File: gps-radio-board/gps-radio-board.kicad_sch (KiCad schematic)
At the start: 21 parts, among them J1 SMA, J2 SMA, J3 USB_C_Receptacle_USB2.0_16P, J4 JST_BATT, U1 ESP32-C6-MINI-1U-H4, U4 AP2112K-3.3, U5 MAX-M10N, U6 MCP73831, U7 AP2112K-3.3

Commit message: Add components to schematic
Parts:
- added C10: 22u, Capacitor_SMD:C_0603_1608Metric_Pad1.08x0.95mm_HandSolder, symbol Device:C
- added C7: 1u, Capacitor_SMD:C_0603_1608Metric_Pad1.08x0.95mm_HandSolder, symbol Device:C
- added C8, C9: 100n, Capacitor_SMD:C_0603_1608Metric_Pad1.08x0.95mm_HandSolder, symbol Device:C
- added D2: LED, LED_SMD:LED_0201_0603Metric_Pad0.64x0.40mm_HandSolder, symbol Device:LED
- added R5: 470, Resistor_SMD:R_0603_1608Metric_Pad0.98x0.95mm_HandSolder, symbol Device:R_US
- added R6, R7: 10k, Resistor_SMD:R_0603_1608Metric_Pad0.98x0.95mm_HandSolder, symbol Device:R_US
- added RST2: SW_Omron_B3FS, Button_Switch_SMD:SW_SPST_Omron_B3FS-100xP, symbol Switch:SW_Omron_B3FS
- J4: footprint Connector_JST:JST_XH_S2B-XH-A-1_1x02_P2.50mm_Horizontal -> Connector_JST:JST_GH_SM02B-GHS-TB_1x02-1MP_P1.25mm_Horizontal
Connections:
- net +BATT: no longer U4.3 (EN)
- net GND: now also C10.1, C7.1, C8.2, C9.1, R5.2, RST2.1
- net WIO_UART_2_RX: now also U1.31 (TXD0); no longer U1.30 (RXD0)
- net WIO_UART_2_TX: now also U1.30 (RXD0); no longer U1.31 (TXD0)
- net EXT_INT_GPS: now reaches U5.5 (EXTINT)
- net EXT_INT_GPS: now also U2.20 (PB10)
- net +3V3: now reaches U5.7 (V_IO)
- net +3V3: now also C1.1, C2.1, C3.1, U2.1 (VCC), U2.28 (VDD), U4.5 (VOUT), U5.8 (VCC)
- net at U1.22 (IO8): now also R7.1
- net at U1.5 (IO2): now also U4.3 (EN)
- net at U1.6 (IO3): now also D2.2 (A)
- net at U1.8 (EN): now also C7.2, C8.1, R6.1, RST2.2
- net SPI-CS: now reaches U2.23 (PA0)
- net +3V3_G renamed +3V3_E
- net +3V3_E: now also U1.3 (3V3), C10.2, C9.2, R6.2, R7.2
- removed net +3V3_R: C1.1, C2.1, C3.1, U1.3 (3V3), U2.1 (VCC), U2.28 (VDD), U4.5 (VOUT)
- new net: D2.1 (K), R5.1
- no-connect marks 2 -> 29
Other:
- note added: "<-Connect if active antenna used"
- note added: "Battery Charger"
- note added: "GPS"
- note added: "Radio"
- note added: "\/-Connect if backup supply is wanted"
- moved on the sheet: C2, C3, C4, J1, J2, J4, R3, U2, U5

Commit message: Inital rousting
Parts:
- removed RST2: SW_Omron_B3FS, Button_Switch_SMD:SW_SPST_Omron_B3FS-100xP, symbol Switch:SW_Omron_B3FS
- added C11, C12: 15p, Capacitor_SMD:C_0603_1608Metric_Pad1.08x0.95mm_HandSolder, symbol Device:C
- added D3, D4: 40V@1A, Diode_SMD:D_SOD-123, symbol Device:D_Schottky
- added J5, J6: Conn_01x04, Connector_JST:JST_SH_BM04B-SRSS-TB_1x04-1MP_P1.00mm_Vertical, symbol Connector_Generic:Conn_01x04
- added J7: Conn_01x04, Connector_PinHeader_2.54mm:PinHeader_1x04_P2.54mm_Vertical, symbol Connector_Generic:Conn_01x04
- added R8, R9: 22, Resistor_SMD:R_0603_1608Metric_Pad0.98x0.95mm_HandSolder, symbol Device:R_US
- D1, D2: footprint LED_SMD:LED_0201_0603Metric_Pad0.64x0.40mm_HandSolder -> LED_SMD:LED_0603_1608Metric_Pad1.05x0.95mm_HandSolder
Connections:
- net +3V3: now also J5.1 (Pin_1), J6.3 (Pin_3)
- net +3V3_E: now also J7.1 (Pin_1)
- net +BATT: now also D3.2 (A); no longer C4.1, C5.1, U4.1 (VIN), U7.1 (VIN), U7.3 (EN)
- net GND: now also C11.1, C12.1, J5.4 (Pin_4), J6.4 (Pin_4), J7.4 (Pin_4)
- net I2C-2-SCA: now also J6.2 (Pin_2)
- net I2C-2-SCL: now also J6.1 (Pin_1)
- net SWD-WIO-CLK: now also J5.3 (Pin_3)
- net SWD-WIO-IO: now also J5.2 (Pin_2)
- net USB_D+: now also C11.2, R8.1; no longer J3.A6 (D+), J3.B6 (D+)
- net USB_D-: now also C12.2, R9.1; no longer J3.A7 (D-), J3.B7 (D-)
- net USB_IN: now also D4.2 (A)
- net at U1.10 (IO5): now also J7.3 (Pin_3)
- net at U1.9 (IO4): now also J7.2 (Pin_2)
- new net: J3.A6 (D+), J3.B6 (D+), R8.2
- new net: C4.1, C5.1, D3.1 (K), D4.1 (K), U4.1 (VIN), U7.1 (VIN), U7.3 (EN)
- new net: J3.A7 (D-), J3.B7 (D-), R9.2
- no-connect marks 29 -> 27
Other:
- moved on the sheet: R7

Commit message: Update silkscreen
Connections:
- net +3V3: now also J5.3 (Pin_3); no longer J5.1 (Pin_1)
- net SWD-WIO-CLK: now also J5.2 (Pin_2); no longer J5.3 (Pin_3)
- net SWD-WIO-IO: now also J5.1 (Pin_1); no longer J5.2 (Pin_2)
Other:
- moved on the sheet: J5
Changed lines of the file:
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@@
 	(wire
 		(pts
+			(xy 591.82 363.22) (xy 594.36 363.22)
+		)
+		(stroke
+			(width 0)
+			(type default)
+		)
+	)
+	(wire
+		(pts
+			(xy 598.17 365.76) (xy 591.82 365.76)
+		)
+		(stroke
+			(width 0)
+			(type default)
+		)
+	)
+	(wire
+		(pts
 			(xy 676.91 228.6) (xy 679.45 228.6)
 		)
@@
 	(wire
 		(pts
-			(xy 590.55 359.41) (xy 594.36 359.41)
-		)
-		(stroke
-			(width 0)
-			(type default)
-		)
-	)
-	(wire
-		(pts
 			(xy 477.52 359.41) (xy 477.52 361.95)
 		)
@@
 	(wire
 		(pts
-			(xy 590.55 356.87) (xy 593.09 356.87)
-		)
-		(stroke
-			(width 0)
-			(type default)
-		)
-	)
-	(wire
-		(pts
 			(xy 571.5 299.72) (xy 565.15 299.72)
 		)
@@
 	(wire
 		(pts
-			(xy 593.09 353.06) (xy 622.3 353.06)
+			(xy 591.82 353.06) (xy 622.3 353.06)
 		)
 		(stroke
@@
 	(wire
 		(pts
-			(xy 593.09 356.87) (xy 593.09 353.06)
+			(xy 591.82 360.68) (xy 591.82 353.06)
 		)
 		(stroke
@@
 	(wire
 		(pts
-			(xy 594.36 359.41) (xy 594.36 355.6)
+			(xy 594.36 363.22) (xy 594.36 355.6)
 		)
 		(stroke
@@
 	)
 	(symbol
-		(lib_id "power:+3V3")
-		(at 590.55 354.33 0)
-		(unit 1)
-		(body_style 1)
-		(exclude_from_sim no)
-		(in_bom yes)
-		(on_board yes)
-		(in_pos_files yes)
-		(dnp no)
-		(fields_autoplaced yes)
-		(property "Reference" "#PWR031"
-			(at 590.55 358.14 0)
-			(hide yes)
-			(show_name no)
-			(do_not_autoplace no)
-			(effects
-				(font
-					(size 1.27 1.27)
-				)
-			)
-		)
-		(property "Value" "+3V3"
-			(at 590.55 349.25 0)
-			(show_name no)
-			(do_not_autoplace no)
-			(effects
-				(font
-					(size 1.27 1.27)
-				)
-			)
-		)
-		(property "Footprint" ""
-			(at 590.55 354.33 0)
-			(hide yes)
-			(show_name no)
-			(do_not_autoplace no)
-			(effects
-				(font
-					(size 1.27 1.27)
-				)
-			)
-		)
-		(property "Datasheet" ""
-			(at 590.55 354.33 0)
-			(hide yes)
-			(show_name no)
-			(do_not_autoplace no)
-			(effects
-				(font
-					(size 1.27 1.27)
-				)
-			)
-		)
-		(property "Description" "Power symbol creates a global label with name \"+3V3\""
-			(at 590.55 354.33 0)
-			(hide yes)
-			(show_name no)
-			(do_not_autoplace no)
-			(effects
-				(font
-					(size 1.27 1.27)
-				)
-			)
-		)
-		(pin "1"
-		)
-		(instances
-			(project "gps-radio-board"
-				(path "/6516832b-56dd-436b-980b-7ee5d107ab91"
-					(reference "#PWR031")
-					(unit 1)
-				)
-			)
-		)
-	)
-	(symbol
 		(lib_id "Device:D_Schottky")
 		(at 501.65 261.62 180)
@@
 	(symbol
 		(lib_id "PCM_SparkFun-PowerSymbol:GND")
-		(at 590.55 361.95 0)
+		(at 591.82 368.3 0)
 		(unit 1)
 		(body_style 1)
@@
 		(fields_autoplaced yes)
 		(property "Reference" "#PWR032"
-			(at 590.55 368.3 0)
+			(at 591.82 374.65 0)
 			(hide yes)
 			(show_name no)
@@
 		)
 		(property "Value" "GND"
-			(at 590.55 365.76 0)
+			(at 591.82 372.11 0)
 			(show_name no)
 			(do_not_autoplace yes)
@@
 		)
 		(property "Footprint" ""
-			(at 590.55 361.95 0)
+			(at 591.82 368.3 0)
 			(hide yes)
 			(show_name no)
@@
 		)
 		(property "Datasheet" ""
-			(at 590.55 361.95 0)
+			(at 591.82 368.3 0)
 			(hide yes)
 			(show_name no)
@@
 		)
 		(property "Description" "Power symbol creates a global label with name \"GND\" , ground"
-			(at 590.55 370.84 0)
+			(at 591.82 377.19 0)
 			(hide yes)
 			(show_name no)
@@
 	(symbol
 		(lib_id "Connector_Generic:Conn_01x04")
-		(at 585.47 356.87 0)
+		(at 586.74 363.22 0)
 		(mirror y)
 		(unit 1)
@@
 		(dnp no)
 		(property "Reference" "J5"
-			(at 580.644 348.742 0)
+			(at 581.914 355.092 0)
 			(show_name no)
 			(do_not_autoplace no)
@@
 		)
 		(property "Value" "Conn_01x04"
-			(at 580.644 351.028 0)
+			(at 581.914 357.378 0)
 			(show_name no)
 			(do_not_autoplace no)
@@
 		)
 		(property "Footprint" "Connector_JST:JST_SH_BM04B-SRSS-TB_1x04-1MP_P1.00mm_Vertical"
-			(at 585.47 356.87 0)
+			(at 586.74 363.22 0)
 			(hide yes)
 			(show_name no)
@@
 		)
 		(property "Datasheet" ""
-			(at 585.47 356.87 0)
+			(at 586.74 363.22 0)
 			(hide yes)
 			(show_name no)
@@
 		)
 		(property "Description" "Generic connector, single row, 01x04, script generated (kicad-library-utils/schlib/autogen/connector/)"
-			(at 585.47 356.87 0)
+			(at 586.74 363.22 0)
 			(hide yes)
 			(show_name no)
@@
 					(unit 1)
 				)
+			)
+		)
+	)
+	(symbol
+		(lib_id "power:+3V3")
+		(at 598.17 365.76 0)
+		(unit 1)
+		(body_style 1)
+		(exclude_from_sim no)
+		(in_bom yes)
+		(on_board yes)
+		(in_pos_files yes)
+		(dnp no)
+		(fields_autoplaced yes)
+		(property "Reference" "#PWR036"
+			(at 598.17 369.57 0)
+			(hide yes)
+			(show_name no)
+			(do_not_autoplace no)
+			(effects
+				(font
+					(size 1.27 1.27)
+				)
+			)
+		)
+		(property "Value" "+3V3"
+			(at 598.17 360.68 0)
+			(show_name no)
+			(do_not_autoplace no)
+			(effects
+				(font
+					(size 1.27 1.27)
+				)
+			)
+		)
+		(property "Footprint" ""
+			(at 598.17 365.76 0)
+			(hide yes)
+			(show_name no)
+			(do_not_autoplace no)
+			(effects
+				(font
+					(size 1.27 1.27)
+				)
+			)
+		)
+		(property "Datasheet" ""
+			(at 598.17 365.76 0)
+			(hide yes)
+			(show_name no)
+			(do_not_autoplace no)
+			(effects
+				(font
+					(size 1.27 1.27)
+				)
+			)
+		)
+		(property "Description" "Power symbol creates a global label with name \"+3V3\""
+			(at 598.17 365.76 0)
+			(hide yes)
+			(show_name no)
+			(do_not_autoplace no)
+			(effects
+				(font
+					(size 1.27 1.27)
+				)
+			)
+		)
+		(pin "1"
+		)
+		(instances
+			(project "gps-radio-board"
+				(path "/6516832b-56dd-436b-980b-7ee5d107ab91"
+					(reference "#PWR036")
+					(unit 1)
+				)

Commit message: Update silkscreen
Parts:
- added D5, D6: LED, LED_SMD:LED_0603_1608Metric_Pad1.05x0.95mm_HandSolder, symbol Device:LED
- added R10, R11: 470, Resistor_SMD:R_0603_1608Metric_Pad0.98x0.95mm_HandSolder, symbol Device:R_US
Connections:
- net GND: now also R10.2, R11.2
- net at U2.21 (PA9): now also D6.2 (A)
- net at U2.27 (PA10): now also D5.2 (A)
- new net: D5.1 (K), R10.1
- new net: D6.1 (K), R11.1
- no-connect marks 27 -> 25

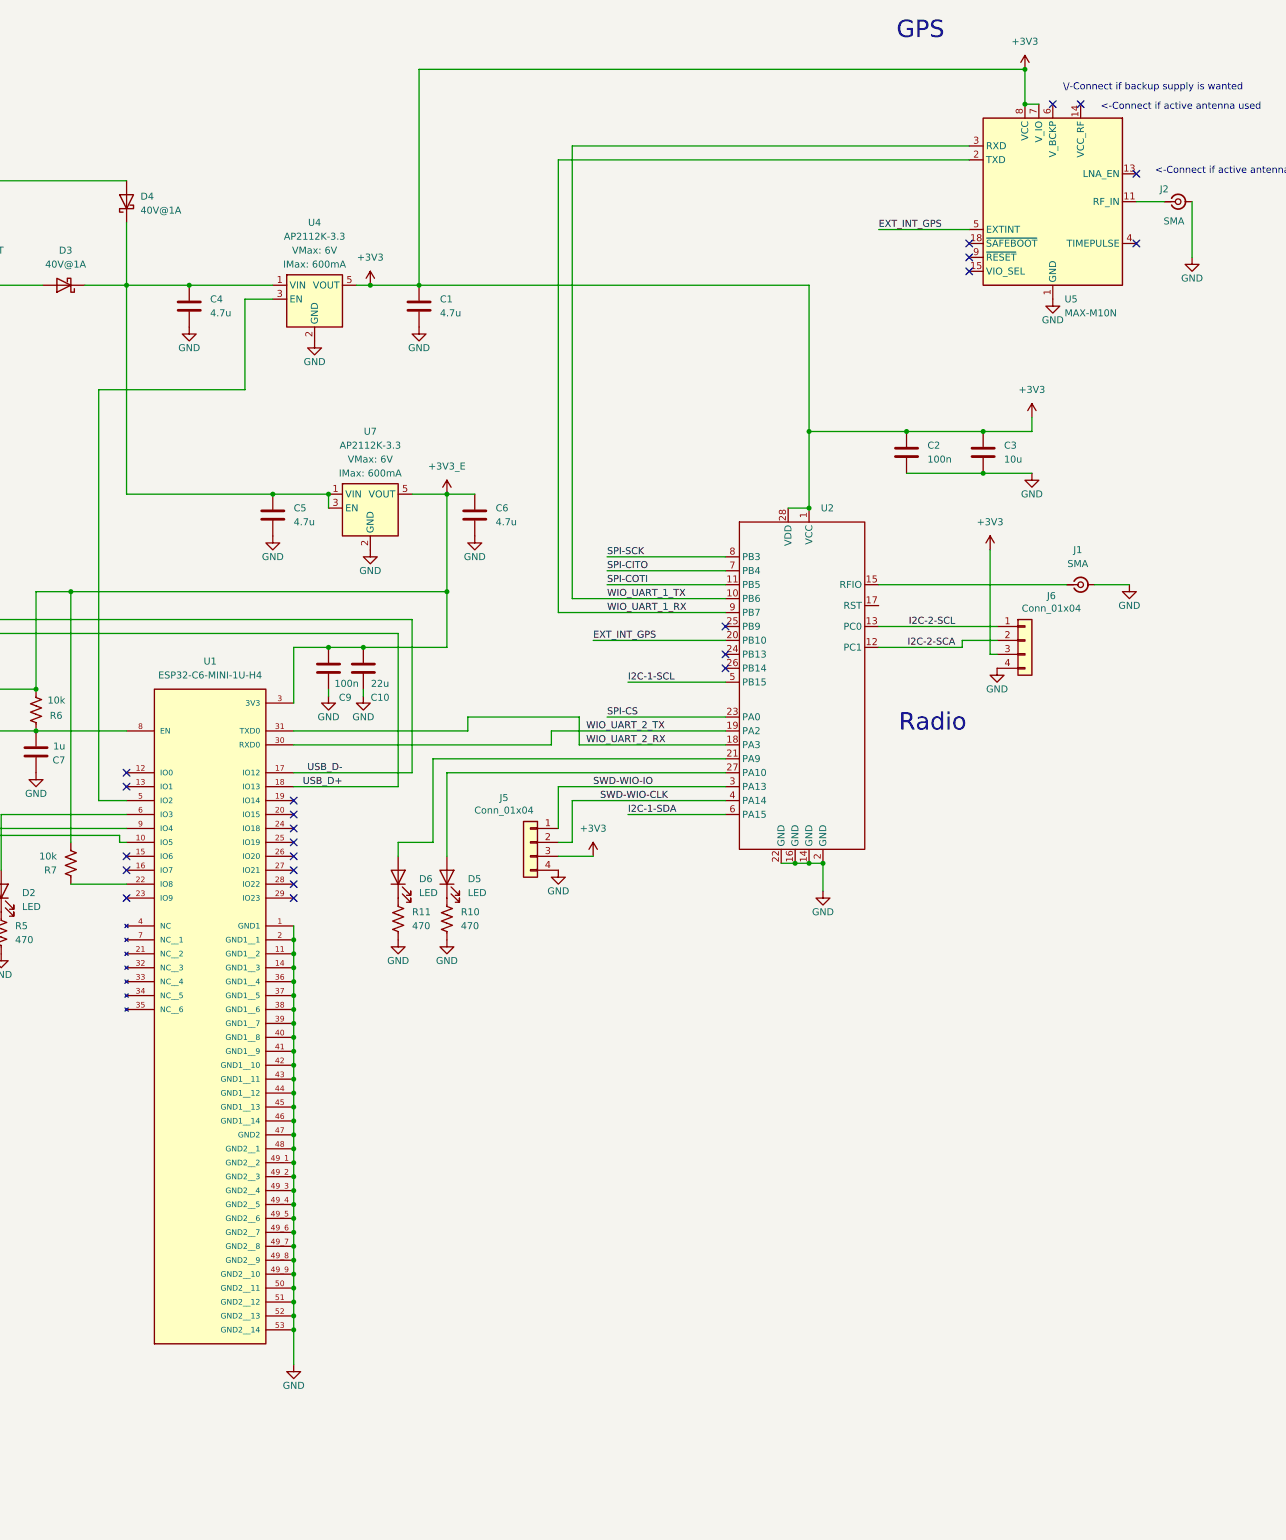
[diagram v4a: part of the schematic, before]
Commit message: Add leds. Add current ratings
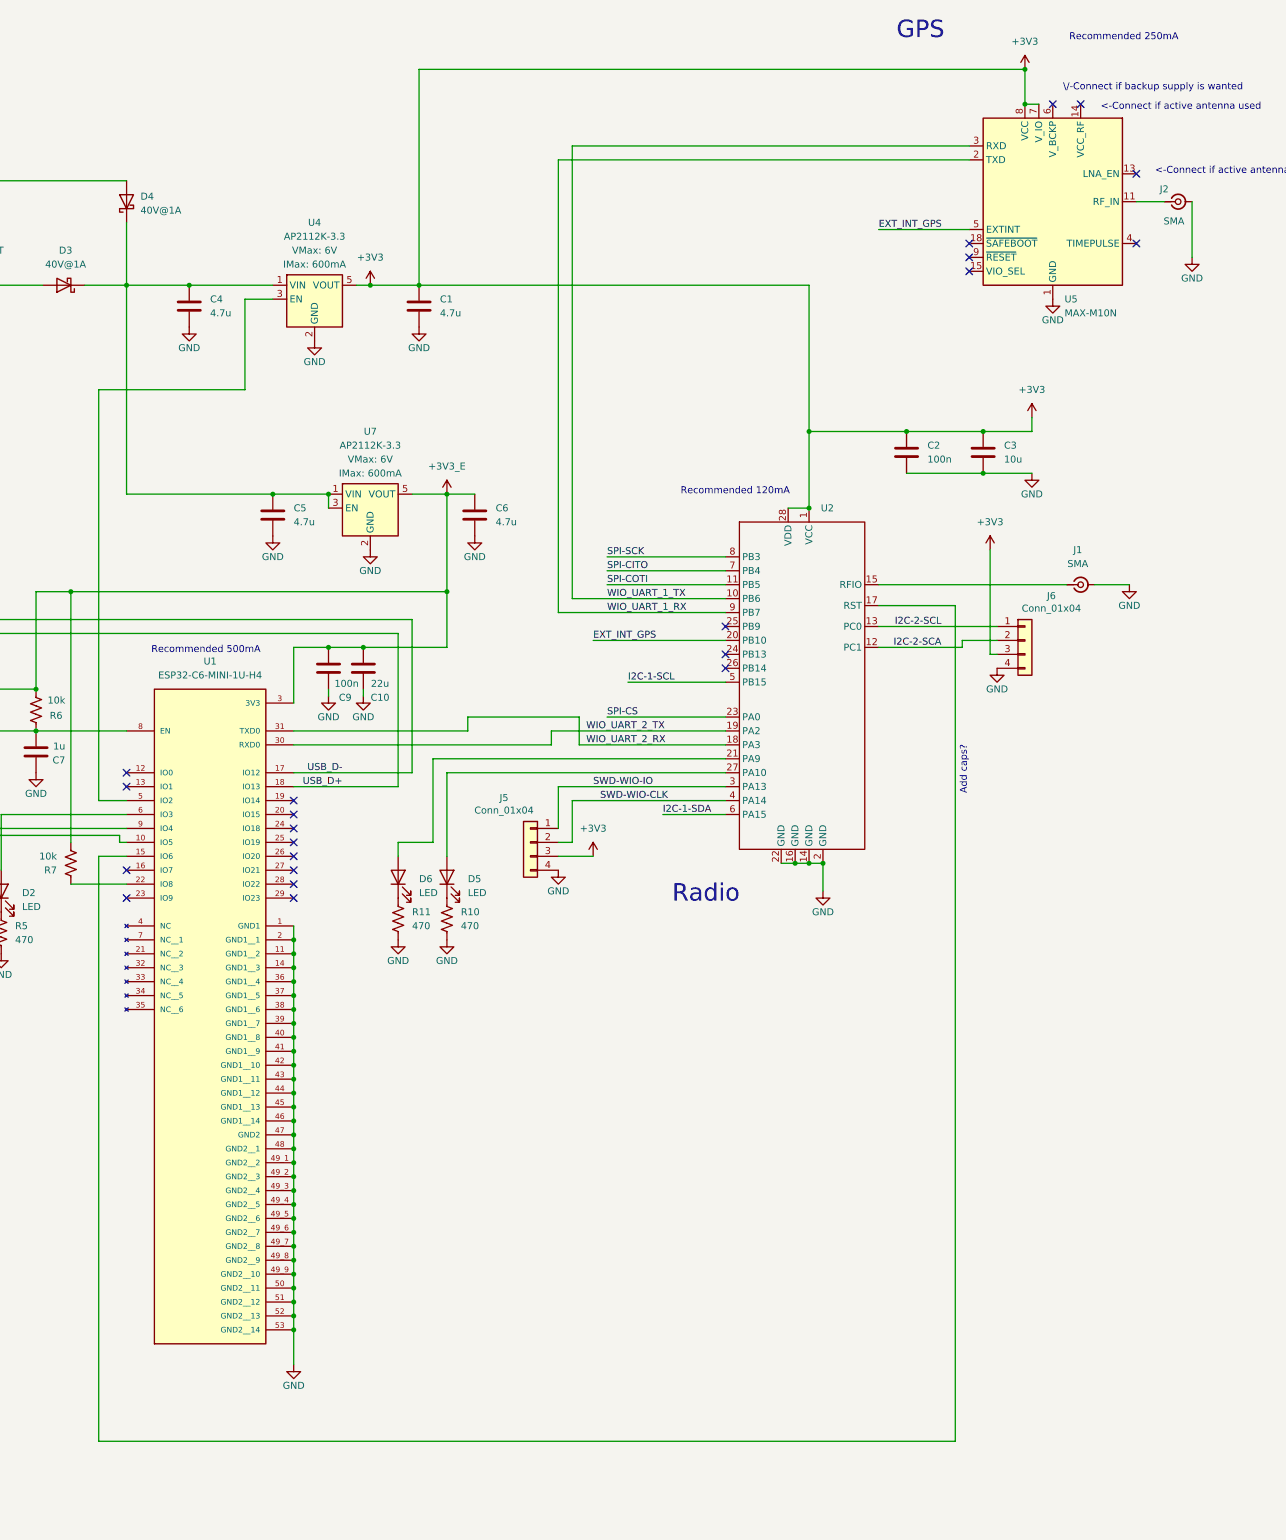
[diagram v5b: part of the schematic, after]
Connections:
- net at U1.15 (IO6): now also U2.17 (RST)
- no-connect marks 25 -> 24
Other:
- note added: "Add caps?"
- note added: "Recommended 120mA"
- note added: "Recommended 250mA"
- note added: "Recommended 500mA"
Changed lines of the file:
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@@
 	(text "Radio"
 		(exclude_from_sim no)
-		(at 660.0892 341.428 0)
+		(at 618.744 372.618 0)
 		(effects
 			(font
@@
 		)
 	)
+	(text "Recommended 120mA"
+		(exclude_from_sim no)
+		(at 624.078 299.212 0)
+		(effects
+			(font
+				(size 1.27 1.27)
+			)
+		)
+	)
 	(text "<-Connect if active antenna used\n"
 		(exclude_from_sim no)
@@
 		)
 	)
+	(text "Recommended 500mA"
+		(exclude_from_sim no)
+		(at 527.558 328.168 0)
+		(effects
+			(font
+				(size 1.27 1.27)
+			)
+		)
+	)
 	(text "GPS"
 		(exclude_from_sim no)
@@
 		)
 	)
+	(text "Add caps?"
+		(exclude_from_sim no)
+		(at 665.734 350.012 90)
+		(effects
+			(font
+				(size 1.27 1.27)
+			)
+		)
+	)
+	(text "Recommended 250mA"
+		(exclude_from_sim no)
+		(at 694.944 216.408 0)
+		(effects
+			(font
+				(size 1.27 1.27)
+			)
+		)
+	)
 	(text "Battery Charger\n"
 		(exclude_from_sim no)
@@
 	)
 	(no_connect
-		(at 513.08 365.76)
-	)
-	(no_connect
 		(at 513.08 368.3)
 	)
@@
 	(wire
 		(pts
+			(xy 650.24 327.66) (xy 665.48 327.66)
+		)
+		(stroke
+			(width 0)
+			(type default)
+		)
+	)
+	(wire
+		(pts
 			(xy 600.71 311.15) (xy 622.3 311.15)
 		)
@@
 	(wire
 		(pts
+			(xy 513.08 365.76) (xy 508 365.76)
+		)
+		(stroke
+			(width 0)
+			(type default)
+		)
+	)
+	(wire
+		(pts
 			(xy 457.2 325.12) (xy 458.47 325.12)
 		)
@@
 	(wire
 		(pts
+			(xy 664.21 472.44) (xy 664.21 320.04)
+		)
+		(stroke
+			(width 0)
+			(type default)
+		)
+	)
+	(wire
+		(pts
 			(xy 524.51 261.62) (xy 539.75 261.62)
 		)
@@
 	(wire
 		(pts
+			(xy 508 472.44) (xy 664.21 472.44)
+		)
+		(stroke
+			(width 0)
+			(type default)
+		)
+	)
+	(wire
+		(pts
 			(xy 480.06 364.49) (xy 480.06 360.68)
 		)
@@
 	(wire
 		(pts
+			(xy 664.21 320.04) (xy 650.24 320.04)
+		)
+		(stroke
+			(width 0)
+			(type default)
+		)
+	)
+	(wire
+		(pts
 			(xy 496.57 317.5) (xy 496.57 335.28)
 		)
@@
 	(wire
 		(pts
-			(xy 665.48 327.66) (xy 650.24 327.66)
-		)
-		(stroke
-			(width 0)
-			(type default)
-		)
-	)
-	(wire
-		(pts
 			(xy 568.96 363.22) (xy 562.61 363.22)
 		)
@@
 	(wire
 		(pts
-			(xy 604.52 358.14) (xy 622.3 358.14)
+			(xy 610.87 358.14) (xy 622.3 358.14)
 		)
 		(stroke
@@
 		(pts
 			(xy 477.52 367.03) (xy 482.6 367.03)
+		)
+		(stroke
+			(width 0)
+			(type default)
+		)
+	)
+	(wire
+		(pts
+			(xy 508 365.76) (xy 508 472.44)
 		)
 		(stroke
@@
 	)
 	(label "I2C-2-SCA"
-		(at 664.21 327.66 180)
+		(at 661.67 327.66 180)
 		(effects
 			(font
@@
 	)
 	(label "I2C-2-SCL"
-		(at 664.21 323.85 180)
+		(at 661.67 323.85 180)
 		(effects
 			(font
@@
 	)
 	(label "I2C-1-SDA"
-		(at 604.52 358.14 0)
+		(at 610.87 358.14 0)
 		(effects
 			(font
